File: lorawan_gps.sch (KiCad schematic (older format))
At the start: 0 parts

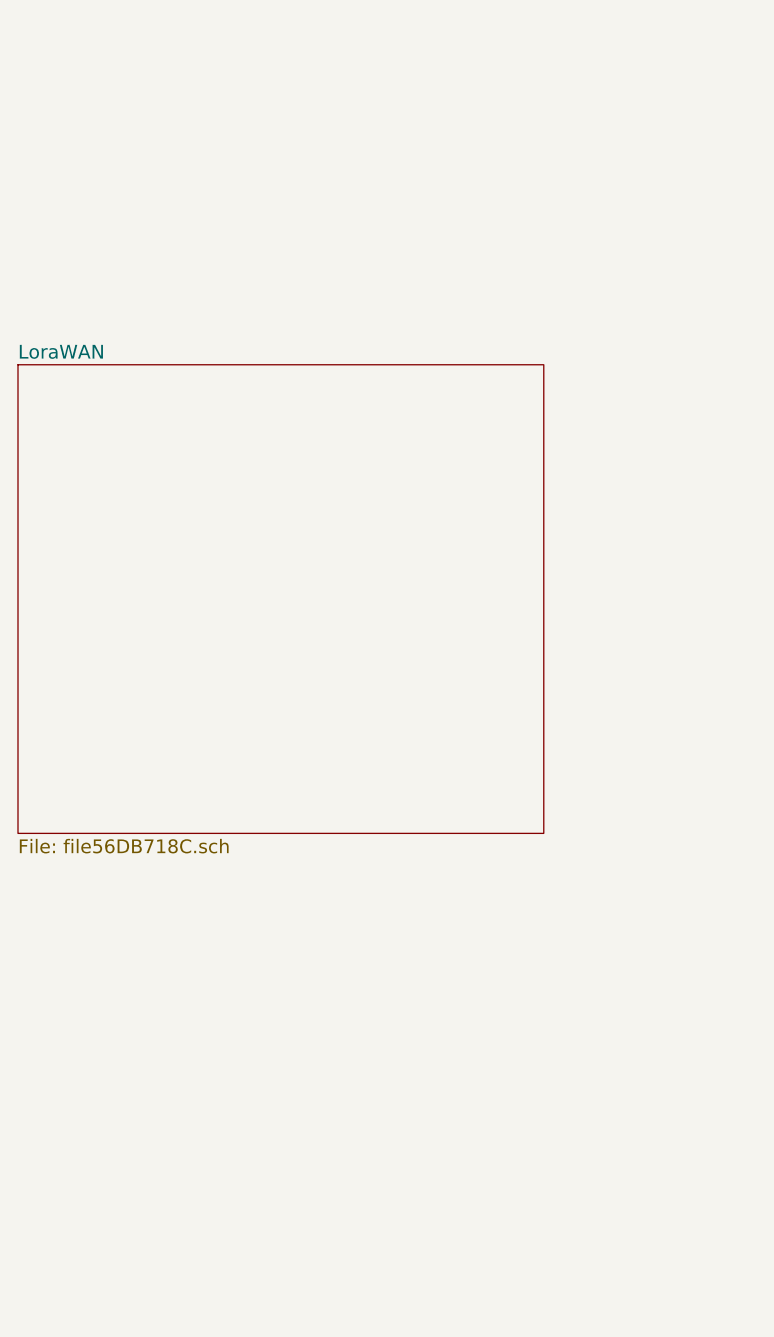
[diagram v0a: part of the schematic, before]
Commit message: Added outline for AAA battery size
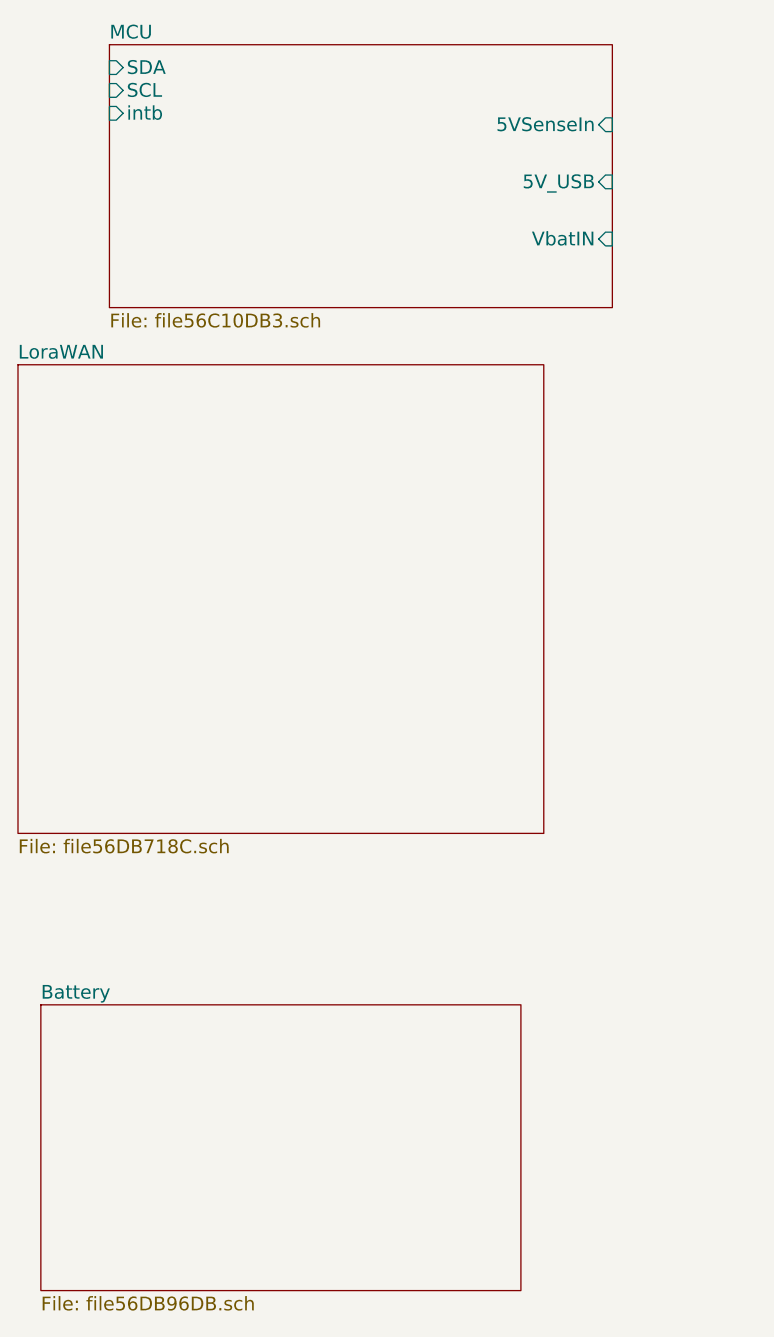
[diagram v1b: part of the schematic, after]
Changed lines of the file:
@@
 LIBS:_sensors
 LIBS:timhawes
+LIBS:SX1276
 LIBS:mpu-9250
-LIBS:SX1276
+LIBS:SAMD21E17A
 LIBS:lorawan_gps-cache
 EELAYER 25 0
@@
 $Descr A4 11693 8268
 encoding utf-8
-Sheet 1 5
+Sheet 1 7
 Title ""
 Date ""
@@
 F1 "file56DB718C.sch" 60
 $EndSheet
+$Sheet
+S 3600 950  2200 1150
+U 56C10DB4
+F0 "MCU" 60
+F1 "file56C10DB3.sch" 60
+F2 "SDA" I L 3600 1050 60
+F3 "SCL" I L 3600 1150 60
+F6 "VbatIN" I R 5800 1800 60
+F7 "5V_USB" I R 5800 1550 60
+F9 "5VSenseIn" I R 5800 1300 60
+F10 "intb" I L 3600 1250 60
+$EndSheet
+$Sheet
+S 3300 5150 2100 1250
+U 56DB96DC
+F0 "Battery" 60
+F1 "file56DB96DB.sch" 60
+$EndSheet
 $EndSCHEMATC

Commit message: started layout, completed schematic
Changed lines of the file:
@@
 LIBS:mpu-9250
 LIBS:SAMD21E17A
+LIBS:miniultrapro
+LIBS:texas-instruments
 LIBS:lorawan_gps-cache
 EELAYER 25 0
@@
 $EndDescr
 $Sheet
-S 7500 1300 1950 1200
+S 1000 2950 1950 1100
+U 56DB6602
+F0 "TempHumidity" 60
+F1 "TempHumidity.sch" 60
+F2 "SDA_TH" B R 2950 3300 60
+F3 "SCL_TH" B R 2950 3450 60
+$EndSheet
+$Sheet
+S 1000 5050 1950 1150
+U 56DB69AB
+F0 "9axis" 60
+F1 "9axis.sch" 60
+F2 "SDA_9AXIS" B R 2950 5300 60
+F3 "SCL_9AXIS" B R 2950 5450 60
+F4 "INT_9AXIS" O R 2950 5600 60
+$EndSheet
+$Sheet
+S 7750 750  1900 2000
+U 56DB718D
+F0 "LoraWAN" 60
+F1 "LoRaWAN.sch" 60
+F2 "RF_RESET" I L 7750 1100 60
+F3 "RF_NSS" I L 7750 1250 60
+F4 "RF_SCLK" I L 7750 1400 60
+F5 "RF_MOSI" I L 7750 1550 60
+F6 "RF_MISO" O L 7750 1700 60
+F7 "RF_DIO0" O L 7750 1900 60
+F8 "RF_DIO1" O L 7750 2100 60
+F9 "RF_DIO2" O L 7750 2300 60
+$EndSheet
+$Sheet
+S 4250 750  2150 2550
+U 56C10DB4
+F0 "MCU" 60
+F1 "MPU.sch" 60
+F2 "MPU_SDA" I L 4250 1350 60
+F3 "MPU_SCL" I L 4250 1500 60
+F4 "VbatIN" I L 4250 3100 60
+F5 "MPU_MOSI" O R 6400 1550 60
+F6 "MPU_MISO" I R 6400 1700 60
+F7 "MPU_SCK" O R 6400 1400 60
+F8 "MPU_SS" O R 6400 1250 60
+F9 "MPU_IN14" I R 6400 2100 60
+F10 "MPU_INT9" I R 6400 1900 60
+F11 "MPU_INT5" I R 6400 2300 60
+F12 "MPU_INT4" I L 4250 1650 60
+F13 "MPU_RX1" I L 4250 1050 60
+F14 "MPU_TX1" O L 4250 1200 60
+F15 "MPU_D14" O R 6400 1100 60
+$EndSheet
+$Sheet
+S 4300 4200 2100 1250
+U 56DB96DC
+F0 "Battery" 60
+F1 "Battery.sch" 60
+F2 "V_BAT" O L 4300 4350 60
+$EndSheet
+$Sheet
+S 1000 800  1950 1050
 U 56DB5747
 F0 "GPS" 60
-F1 "file56DB5746.sch" 60
+F1 "GPS.sch" 60
+F2 "TXD_GPS" O R 2950 1050 60
+F3 "RXD_GPS" I R 2950 1200 60
+F4 "SDA_GPS" I R 2950 1350 60
+F5 "SCL_GPS" I R 2950 1500 60
 $EndSheet
-$Sheet
-S 7400 3000 1950 1350
-U 56DB6602
-F0 "TempHumidity" 60
-F1 "file56DB6601.sch" 60
-$EndSheet
-$Sheet
-S 7750 5000 2000 1250
-U 56DB69AB
-F0 "9axis" 60
-F1 "file56DB69AA.sch" 60
-$EndSheet
-$Sheet
-S 3200 2350 2300 2050
-U 56DB718D
-F0 "LoraWAN" 60
-F1 "file56DB718C.sch" 60
-$EndSheet
-$Sheet
-S 3600 950  2200 1150
-U 56C10DB4
-F0 "MCU" 60
-F1 "file56C10DB3.sch" 60
-F2 "SDA" I L 3600 1050 60
-F3 "SCL" I L 3600 1150 60
-F6 "VbatIN" I R 5800 1800 60
-F7 "5V_USB" I R 5800 1550 60
-F9 "5VSenseIn" I R 5800 1300 60
-F10 "intb" I L 3600 1250 60
-$EndSheet
-$Sheet
-S 3300 5150 2100 1250
-U 56DB96DC
-F0 "Battery" 60
-F1 "file56DB96DB.sch" 60
-$EndSheet
+Wire Wire Line
+	2950 1050 4250 1050
+Wire Wire Line
+	2950 1200 4250 1200
+Wire Wire Line
+	2950 1350 4250 1350
+Wire Wire Line
+	2950 1500 4250 1500
+Wire Wire Line
+	2950 3300 3300 3300
+Wire Wire Line
+	3300 1350 3300 5300
+Connection ~ 3300 1350
+Wire Wire Line
+	2950 3450 3500 3450
+Wire Wire Line
+	3500 1500 3500 5450
+Connection ~ 3500 1500
+Wire Wire Line
+	3300 5300 2950 5300
+Connection ~ 3300 3300
+Wire Wire Line
+	3500 5450 2950 5450
+Connection ~ 3500 3450
+Wire Wire Line
+	2950 5600 3700 5600
+Wire Wire Line
+	3700 5600 3700 1650
+Wire Wire Line
+	3700 1650 4250 1650
+Wire Wire Line
+	6400 1100 7750 1100
+Wire Wire Line
+	6400 1250 7750 1250
+Wire Wire Line
+	6400 1400 7750 1400
+Wire Wire Line
+	6400 1550 7750 1550
+Wire Wire Line
+	6400 1700 7750 1700
+Wire Wire Line
+	6400 1900 7750 1900
+Wire Wire Line
+	6400 2100 7750 2100
+Wire Wire Line
+	6400 2300 7750 2300
+Wire Wire Line
+	4000 3100 4250 3100
+Wire Wire Line
+	4000 3100 4000 4350
+Wire Wire Line
+	4000 4350 4300 4350
 $EndSCHEMATC

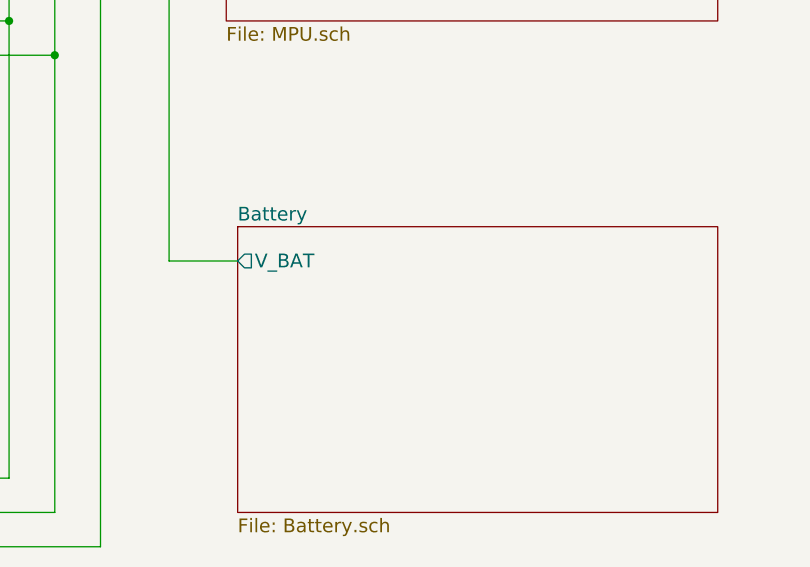
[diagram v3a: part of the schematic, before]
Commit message: Started work to add the power mux and USB connector
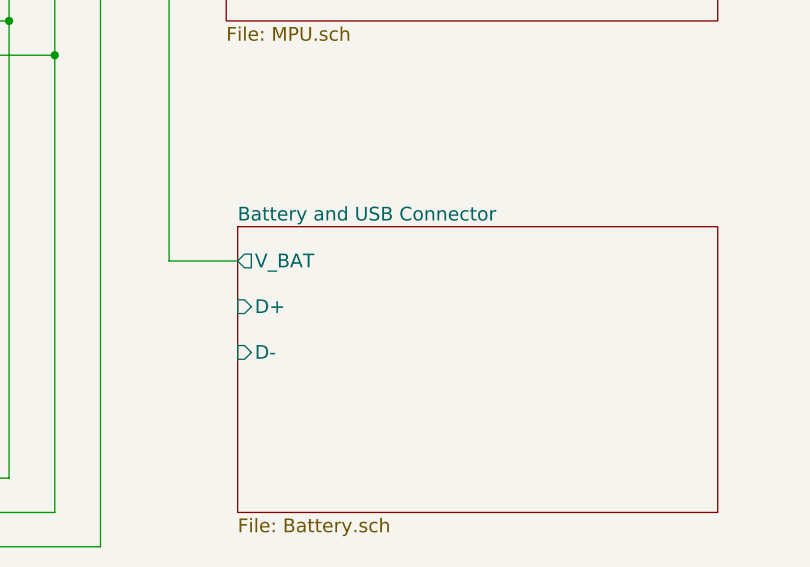
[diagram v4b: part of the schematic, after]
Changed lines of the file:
@@
 S 4300 4200 2100 1250
 U 56DB96DC
-F0 "Battery" 60
+F0 "Battery and USB Connector" 60
 F1 "Battery.sch" 60
 F2 "V_BAT" O L 4300 4350 60
+F3 "D+" I L 4300 4550 60
+F4 "D-" I L 4300 4750 60
 $EndSheet
 $Sheet

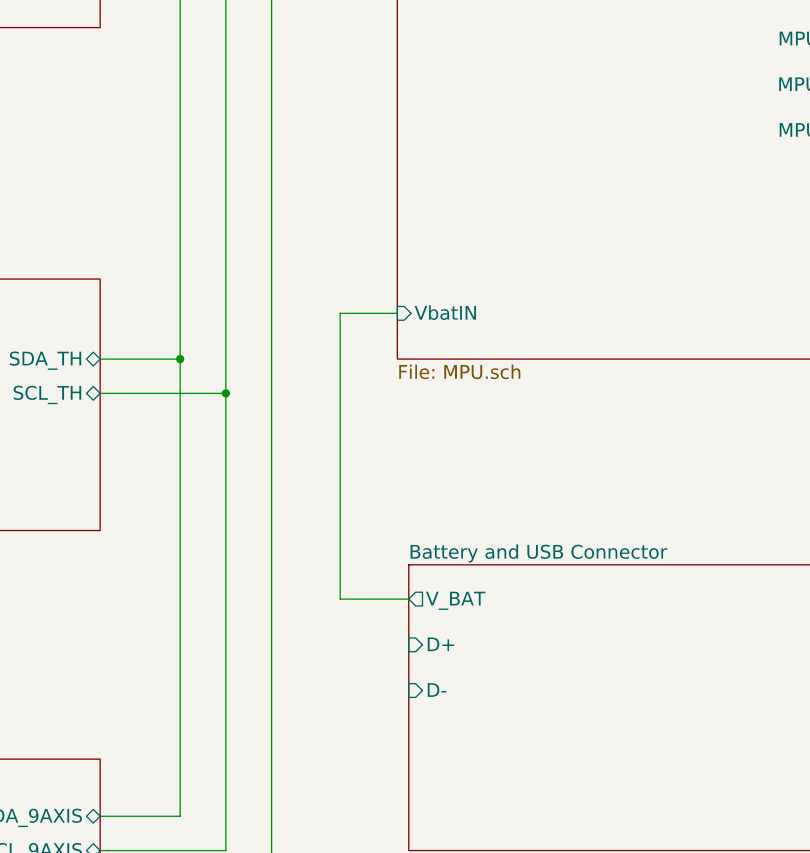
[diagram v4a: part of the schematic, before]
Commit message: Added USB connector, diode or etc to layout@
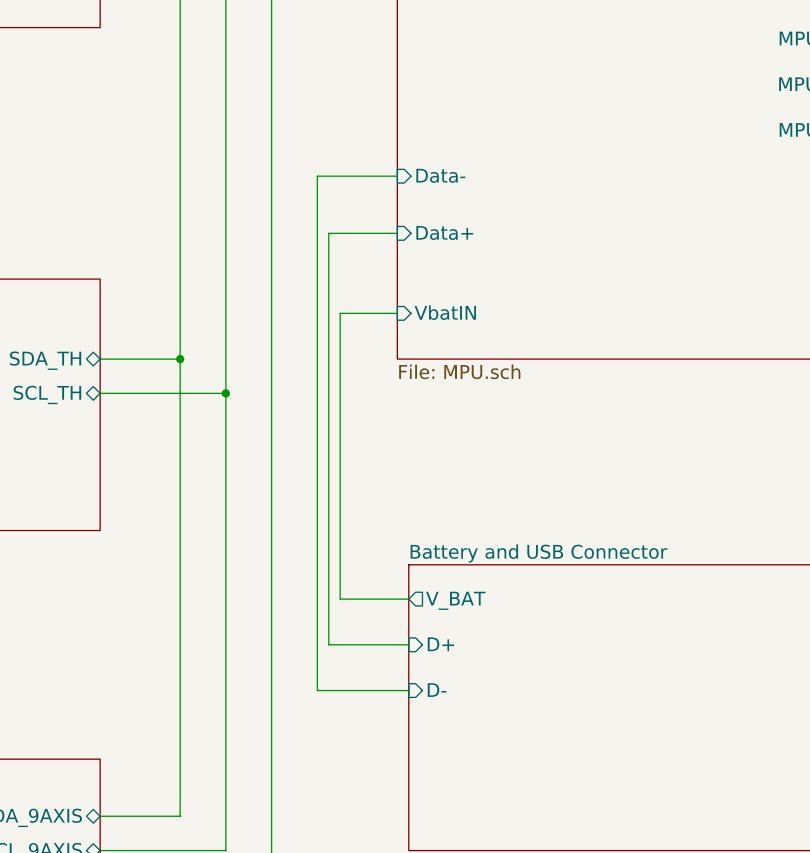
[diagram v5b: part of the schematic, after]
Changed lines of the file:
@@
 F14 "MPU_TX1" O L 4250 1200 60
 F15 "MPU_D14" O R 6400 1100 60
+F16 "Data-" I L 4250 2500 60
+F17 "Data+" I L 4250 2750 60
 $EndSheet
 $Sheet
@@
 Wire Wire Line
 	4000 4350 4300 4350
+Wire Wire Line
+	3950 2750 3950 4550
+Wire Wire Line
+	3950 4550 4300 4550
+Wire Wire Line
+	4250 2500 3900 2500
+Wire Wire Line
+	3900 2500 3900 4750
+Wire Wire Line
+	3900 4750 4300 4750
+Wire Wire Line
+	3950 2750 4250 2750
 $EndSCHEMATC

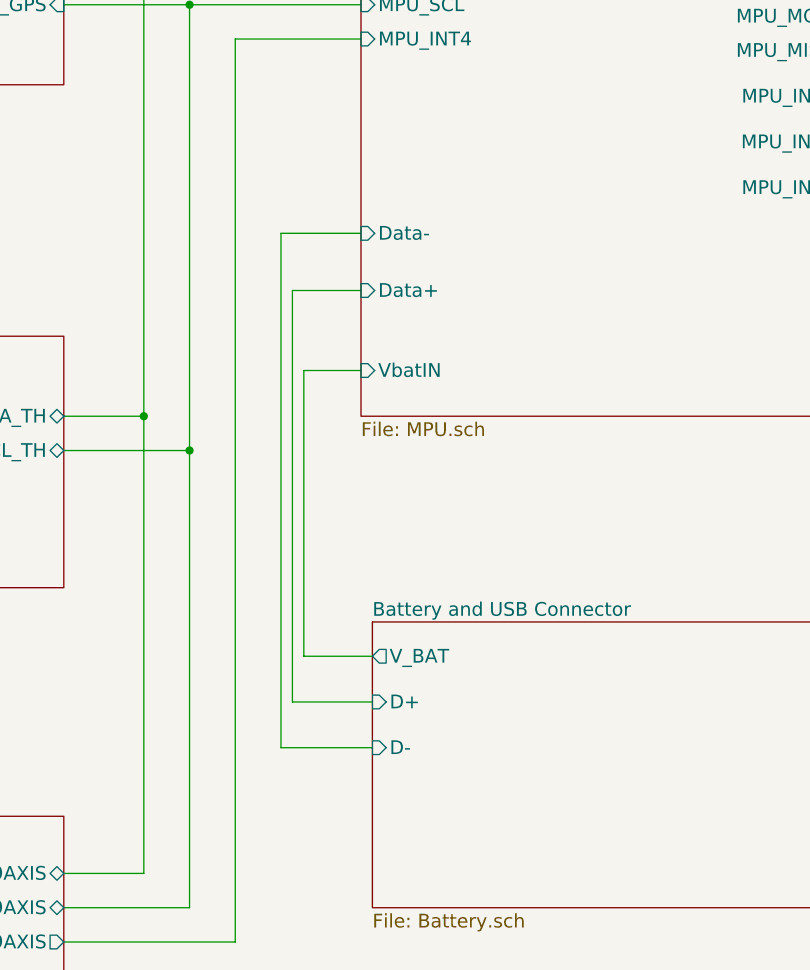
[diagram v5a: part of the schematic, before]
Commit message: Added USB monitoring resistors, still need to set values. Also added stitching vias and tried to clean up some layout
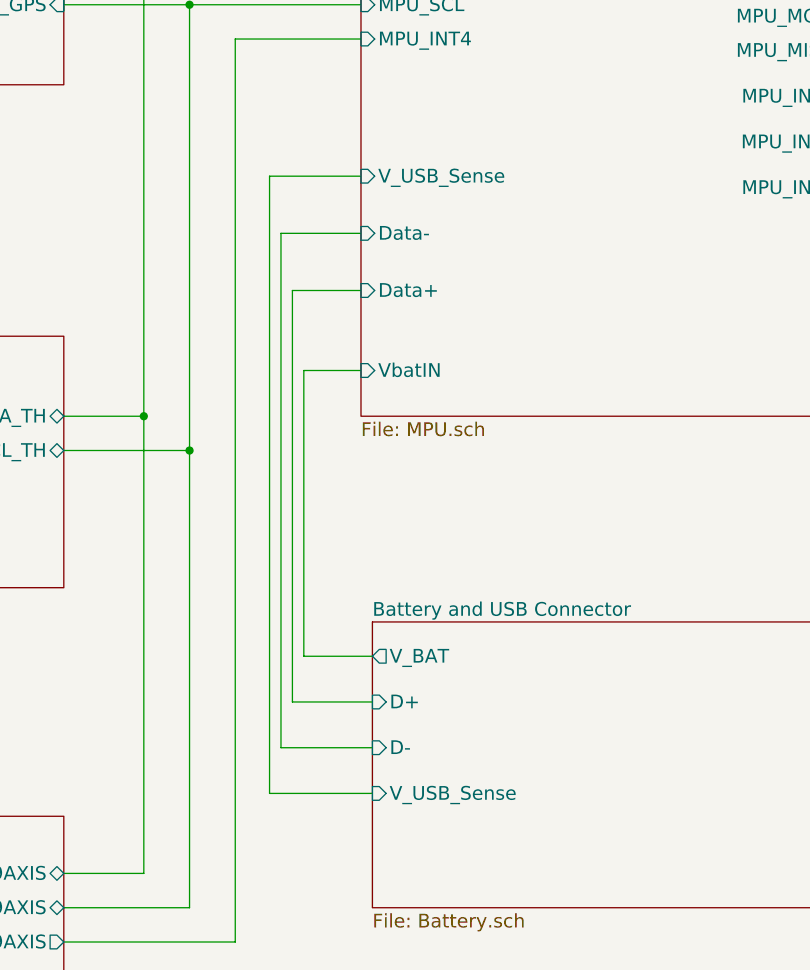
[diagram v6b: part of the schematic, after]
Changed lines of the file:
@@
 F16 "Data-" I L 4250 2500 60
 F17 "Data+" I L 4250 2750 60
+F18 "V_USB_Sense" I L 4250 2250 60
 $EndSheet
 $Sheet
@@
 F3 "D+" I L 4300 4550 60
 F4 "D-" I L 4300 4750 60
+F5 "V_USB_Sense" I L 4300 4950 60
 $EndSheet
 $Sheet
@@
 Wire Wire Line
 	3950 2750 4250 2750
+Wire Wire Line
+	4250 2250 3850 2250
+Wire Wire Line
+	3850 2250 3850 4950
+Wire Wire Line
+	3850 4950 4300 4950
 $EndSCHEMATC
